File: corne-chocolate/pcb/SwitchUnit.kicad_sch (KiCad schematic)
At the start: 4 parts, among them SW1 1U

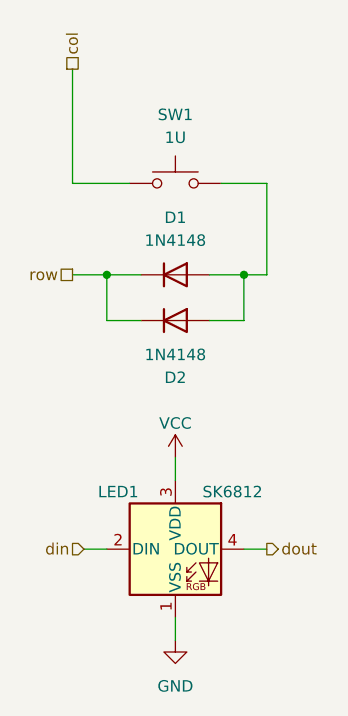
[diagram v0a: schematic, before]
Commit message: pcb remove per-switch LEDs
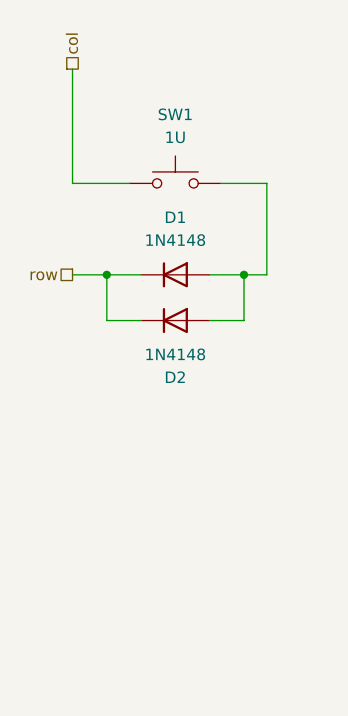
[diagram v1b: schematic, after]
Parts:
- removed LED1: SK6812, corne-chocolate:SK6812MINI-E_doublesided, symbol LED:SK6812
